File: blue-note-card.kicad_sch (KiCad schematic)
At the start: 22 parts, among them J17 N_GR1, J3 MDT420E01001, J7 SF72S006VBAR2500

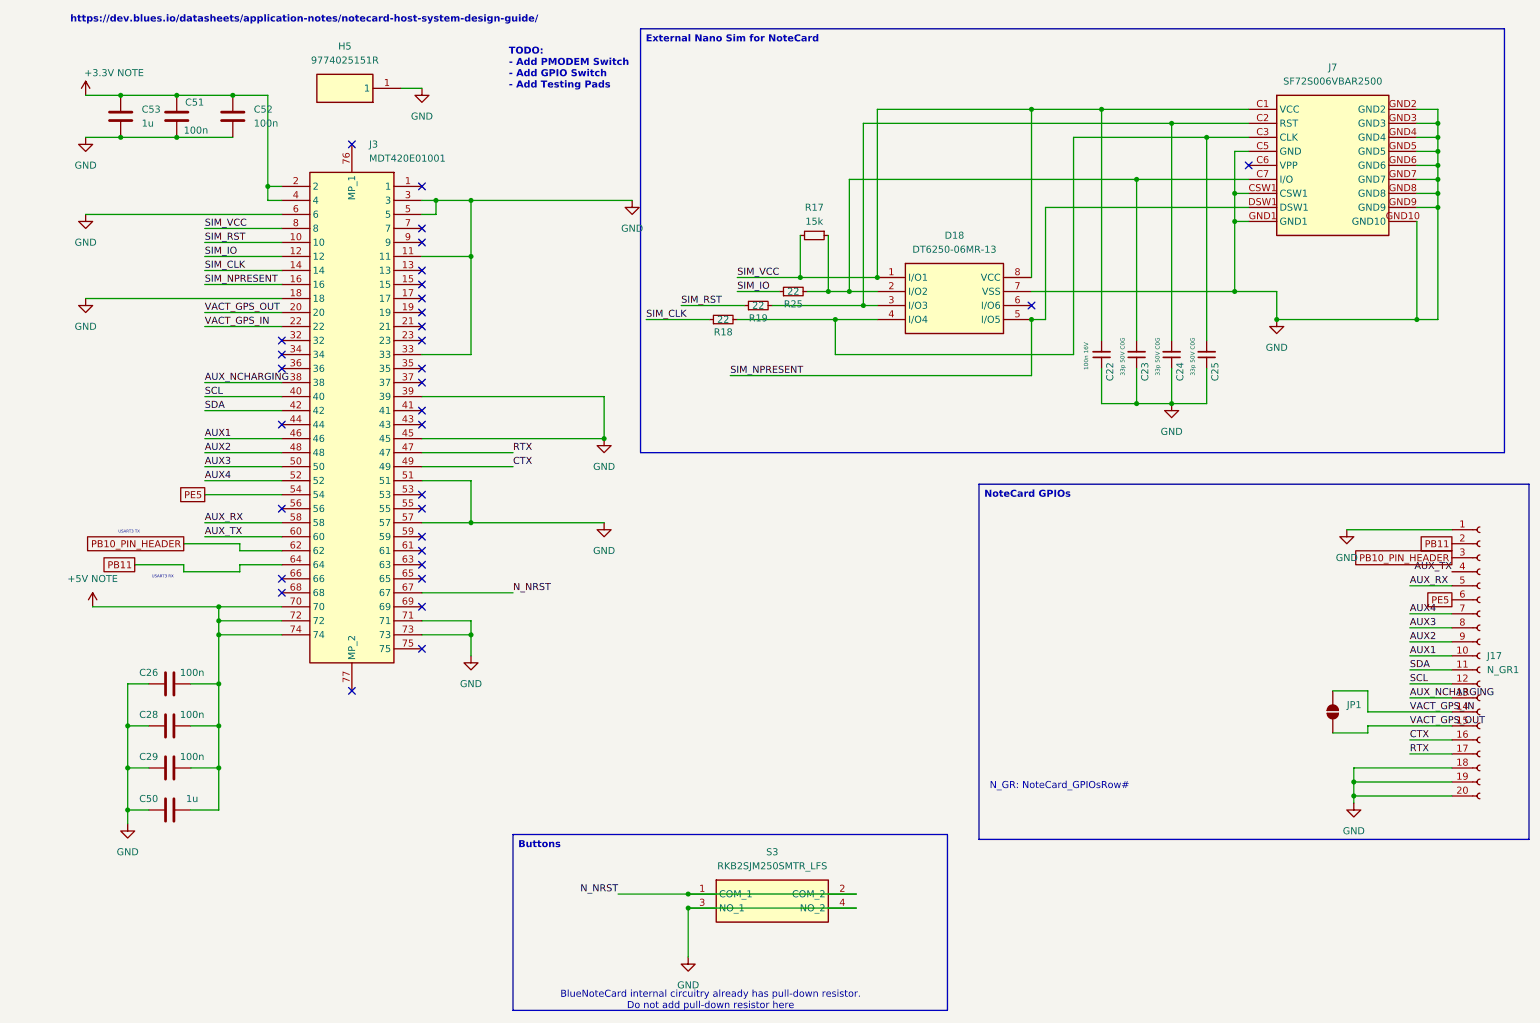
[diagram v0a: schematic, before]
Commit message: Added AUX_EN, I2C com to Blues, LED labels
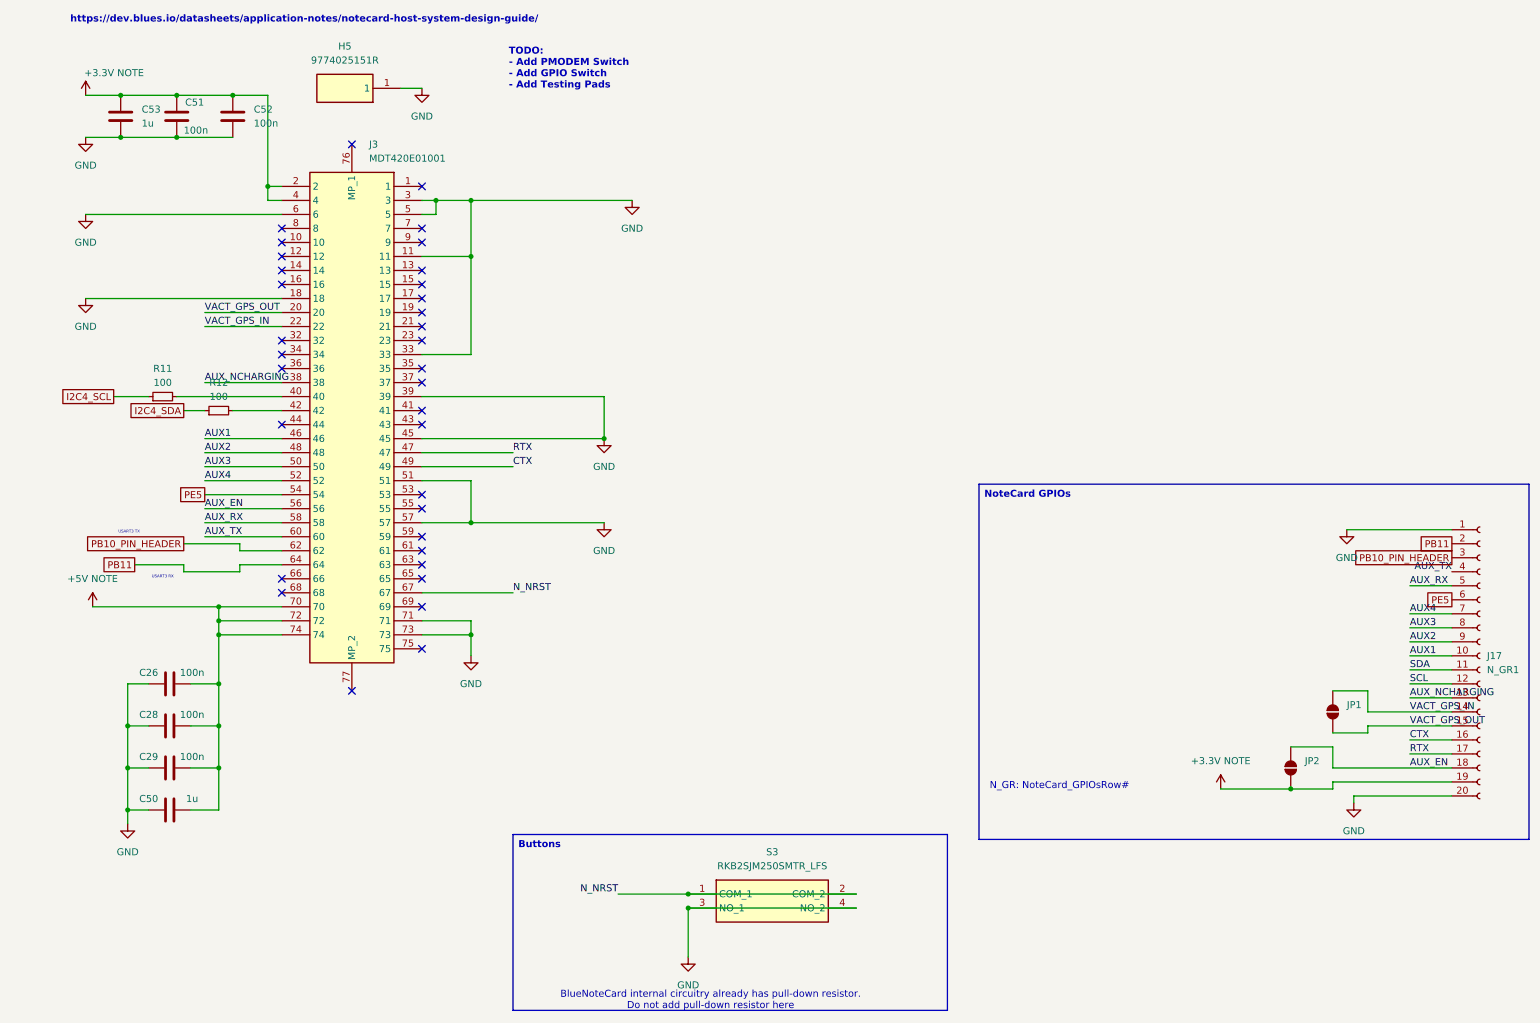
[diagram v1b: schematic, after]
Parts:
- removed C22: 100n 16V, Capacitor_SMD:C_0603_1608Metric_Pad1.08x0.95mm_HandSolder, symbol Device:C_Small
- removed C23, C24, C25: 33p 50V C0G, Capacitor_SMD:C_0603_1608Metric_Pad1.08x0.95mm_HandSolder, symbol Device:C_Small
- removed D18: DT6250-06MR-13, SamacSys_Parts:SOP65P490X110-8N, symbol SamacSys_Parts:DT6250-06MR-13
- removed J7: SF72S006VBAR2500, SamacSys_Parts:SF72S006VBAR2500, symbol SamacSys_Parts:SF72S006VBAR2500
- removed R17: 15k, Resistor_SMD:R_0805_2012Metric_Pad1.20x1.40mm_HandSolder, symbol Device:R_Small
- removed R18, R19, R25: 22, Resistor_SMD:R_0603_1608Metric_Pad0.98x0.95mm_HandSolder, symbol Device:R_Small
- added JP2: SolderJumper_2_Open, Jumper:SolderJumper-2_P1.3mm_Open_RoundedPad1.0x1.5mm, symbol Jumper:SolderJumper_2_Open
- added R11, R12: 100, Resistor_SMD:R_0603_1608Metric_Pad0.98x0.95mm_HandSolder, symbol Device:R_Small
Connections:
- net +3.3V NOTE: now also J17.19 (Pin_19), JP2.2 (B)
- net GND: no longer J17.18 (Pin_18), J17.19 (Pin_19)
- net SCL: no longer J3.40
- net SDA: no longer J3.42
- net AUX_EN: now reaches J3.56
- net AUX_EN: now also J17.18 (Pin_18), JP2.1 (A)
- net SIM_CLK: no longer names the net of J3.14
- net SIM_IO: no longer names the net of J3.12
- net SIM_NPRESENT: no longer names the net of J3.16
- net SIM_RST: no longer names the net of J3.10
- net SIM_VCC: no longer names the net of J3.8
- new net: J3.40, R11.2
- new net: J3.42, R12.2
- new net I2C4_SCL: R11.1
- new net I2C4_SDA: R12.1
- no-connect marks 32 -> 34

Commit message: Added module LEDs, I2C for Blues Com
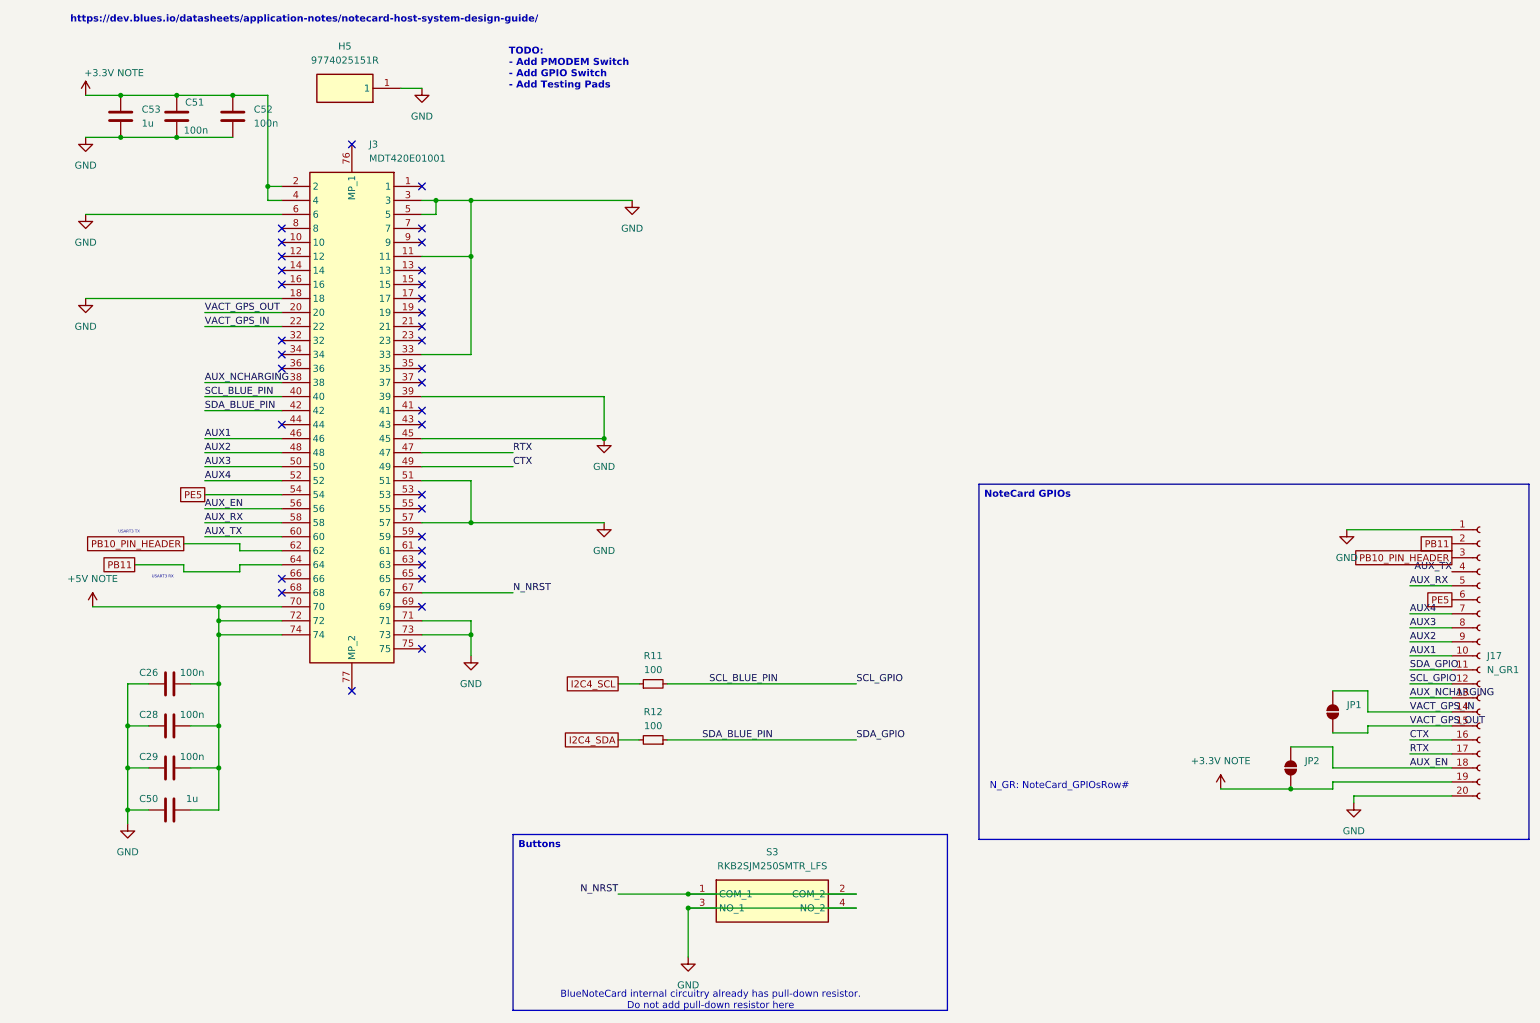
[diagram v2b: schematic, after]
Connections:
- net SCL is gone; now on net SCL_BLUE_PIN: J17.12 (Pin_12)
- net SDA is gone; now on net SDA_BLUE_PIN: J17.11 (Pin_11)
- net I2C4_SDA: now also R12.2; no longer R12.1
- net SCL_BLUE_PIN: now reaches J3.40, R11.2
- net SDA_BLUE_PIN: now reaches J3.42
- net SDA_BLUE_PIN: now also R12.1; no longer R12.2
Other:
- moved on the sheet: R11, R12
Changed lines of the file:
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@@
-	(wire
-		(pts
-			(xy 36.83 87.63) (xy 40.64 87.63)
-		)
-		(stroke
-			(width 0)
-			(type default)
-		)
-	)
 	(wire
 		(pts
@@
 	(wire
 		(pts
+			(xy 115.57 137.16) (xy 119.38 137.16)
+		)
+		(stroke
+			(width 0)
+			(type default)
+		)
+	)
+	(wire
+		(pts
 			(xy 54.61 102.87) (xy 40.64 102.87)
 		)
@@
 	(wire
 		(pts
-			(xy 35.56 85.09) (xy 54.61 85.09)
-		)
-		(stroke
-			(width 0)
-			(type default)
-		)
-	)
-	(wire
-		(pts
 			(xy 80.01 120.65) (xy 96.52 120.65)
 		)
@@
 	(wire
 		(pts
+			(xy 54.61 85.09) (xy 40.64 85.09)
+		)
+		(stroke
+			(width 0)
+			(type default)
+		)
+	)
+	(wire
+		(pts
+			(xy 124.46 137.16) (xy 158.75 137.16)
+		)
+		(stroke
+			(width 0)
+			(type default)
+		)
+	)
+	(wire
+		(pts
 			(xy 88.9 128.27) (xy 88.9 132.08)
 		)
@@
 	(wire
 		(pts
+			(xy 115.57 147.32) (xy 119.38 147.32)
+		)
+		(stroke
+			(width 0)
+			(type default)
+		)
+	)
+	(wire
+		(pts
 			(xy 40.64 72.39) (xy 54.61 72.39)
 		)
@@
 	(wire
 		(pts
-			(xy 24.13 85.09) (xy 30.48 85.09)
-		)
-		(stroke
-			(width 0)
-			(type default)
-		)
-	)
-	(wire
-		(pts
 			(xy 80.01 92.71) (xy 113.03 92.71)
 		)
@@
 	(wire
 		(pts
+			(xy 40.64 87.63) (xy 54.61 87.63)
+		)
+		(stroke
+			(width 0)
+			(type default)
+		)
+	)
+	(wire
+		(pts
 			(xy 88.9 59.69) (xy 88.9 49.53)
 		)
@@
 	(wire
 		(pts
-			(xy 45.72 87.63) (xy 54.61 87.63)
-		)
-		(stroke
-			(width 0)
-			(type default)
-		)
-	)
-	(wire
-		(pts
 			(xy 25.4 38.1) (xy 19.05 38.1)
 		)
@@
 	(wire
 		(pts
+			(xy 124.46 147.32) (xy 158.75 147.32)
+		)
+		(stroke
+			(width 0)
+			(type default)
+		)
+	)
+	(wire
+		(pts
 			(xy 54.61 97.79) (xy 40.64 97.79)
 		)
@@
 			(width 0)
 			(type default)
+		)
+	)
+	(label "SCL_BLUE_PIN"
+		(at 132.08 137.16 0)
+		(effects
+			(font
+				(size 1.27 1.27)
+			)
+			(justify left bottom)
 		)
 	)
@@
 		)
 	)
+	(label "SCL_GPIO"
+		(at 158.75 137.16 0)
+		(effects
+			(font
+				(size 1.27 1.27)
+			)
+			(justify left bottom)
+		)
+	)
 	(label "VACT_GPS_IN"
 		(at 40.64 72.39 0)
@@
 		)
 	)
-	(label "SCL"
+	(label "SCL_GPIO"
 		(at 259.08 137.16 0)
 		(effects
@@
 		)
 	)
-	(label "SDA"
+	(label "SDA_GPIO"
 		(at 259.08 134.62 0)
 		(effects
@@
 		)
 	)
+	(label "SDA_GPIO"
+		(at 158.75 147.32 0)
+		(effects
+			(font
+				(size 1.27 1.27)
+			)
+			(justify left bottom)
+		)
+	)
 	(label "AUX_TX"
 		(at 266.7 116.84 180)
@@
 		)
 	)
+	(label "SDA_BLUE_PIN"
+		(at 130.81 147.32 0)
+		(effects
+			(font
+				(size 1.27 1.27)
+			)
+			(justify left bottom)
+		)
+	)
 	(label "AUX_RX"
 		(at 259.08 119.38 0)
@@
 	(label "AUX1"
 		(at 259.08 132.08 0)
+		(effects
+			(font
+				(size 1.27 1.27)
+			)
+			(justify left bottom)
+		)
+	)
+	(label "SDA_BLUE_PIN"
+		(at 40.64 87.63 0)
+		(effects
+			(font
+				(size 1.27 1.27)
+			)
+			(justify left bottom)
+		)
+	)
+	(label "SCL_BLUE_PIN"
+		(at 40.64 85.09 0)
 		(effects
 			(font
@@
 	(global_label "I2C4_SDA"
 		(shape passive)
-		(at 36.83 87.63 180)
+		(at 115.57 147.32 180)
 		(fields_autoplaced yes)
 		(effects
@@
 		)
 		(property "Intersheetrefs" "${INTERSHEET_REFS}"
-			(at 26.1266 87.63 0)
+			(at 104.8666 147.32 0)
 			(effects
 				(font
@@
 	(global_label "I2C4_SCL"
 		(shape passive)
-		(at 24.13 85.09 180)
+		(at 115.57 137.16 180)
 		(fields_autoplaced yes)
 		(effects
@@
 		)
 		(property "Intersheetrefs" "${INTERSHEET_REFS}"
-			(at 13.4871 85.09 0)
+			(at 104.9271 137.16 0)
 			(effects
 				(font
@@
 	(symbol
 		(lib_id "Device:R_Small")
-		(at 33.02 85.09 90)
+		(at 121.92 137.16 90)
 		(unit 1)
 		(exclude_from_sim no)
@@
 		(fields_autoplaced yes)
 		(property "Reference" "R11"
-			(at 33.02 80.01 90)
+			(at 121.92 132.08 90)
 			(effects
 				(font
@@
 		)
 		(property "Value" "100"
-			(at 33.02 82.55 90)
+			(at 121.92 134.62 90)
 			(effects
 				(font
@@
 		)
 		(property "Footprint" "Resistor_SMD:R_0603_1608Metric_Pad0.98x0.95mm_HandSolder"
-			(at 33.02 85.09 0)
+			(at 121.92 137.16 0)
 			(effects
 				(font
@@
 		)
 		(property "Datasheet" "~"
-			(at 33.02 85.09 0)
+			(at 121.92 137.16 0)
 			(effects
 				(font
@@
 		)
 		(property "Description" "Resistor, small symbol"
-			(at 33.02 85.09 0)
+			(at 121.92 137.16 0)
 			(effects
 				(font
@@
 	(symbol
 		(lib_id "Device:R_Small")
-		(at 43.18 87.63 90)
+		(at 121.92 147.32 270)
+		(mirror x)
 		(unit 1)
 		(exclude_from_sim no)
@@
 		(on_board yes)
 		(dnp no)
-		(fields_autoplaced yes)
 		(property "Reference" "R12"
-			(at 43.18 82.55 90)
+			(at 121.92 142.24 90)
 			(effects
 				(font
@@
 		)
 		(property "Value" "100"
-			(at 43.18 85.09 90)
+			(at 121.92 144.78 90)
 			(effects
 				(font
@@
 		)
 		(property "Footprint" "Resistor_SMD:R_0603_1608Metric_Pad0.98x0.95mm_HandSolder"
-			(at 43.18 87.63 0)
+			(at 121.92 147.32 0)
 			(effects
 				(font
@@
 		)
 		(property "Datasheet" "~"
-			(at 43.18 87.63 0)
+			(at 121.92 147.32 0)
 			(effects
 				(font
@@
 		)
 		(property "Description" "Resistor, small symbol"
-			(at 43.18 87.63 0)
-			(effects
-				(font
+			(at 121.92 147.32 0)
+			(effects
+				(font

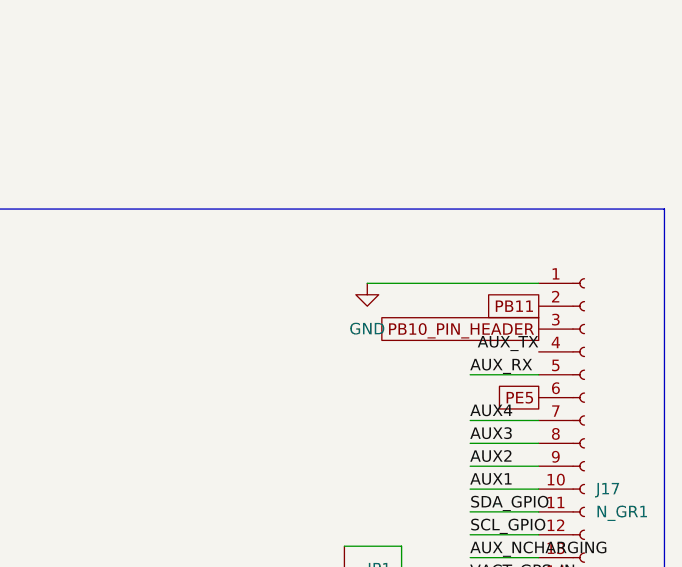
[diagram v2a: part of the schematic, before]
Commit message: Fixed SD Card layout
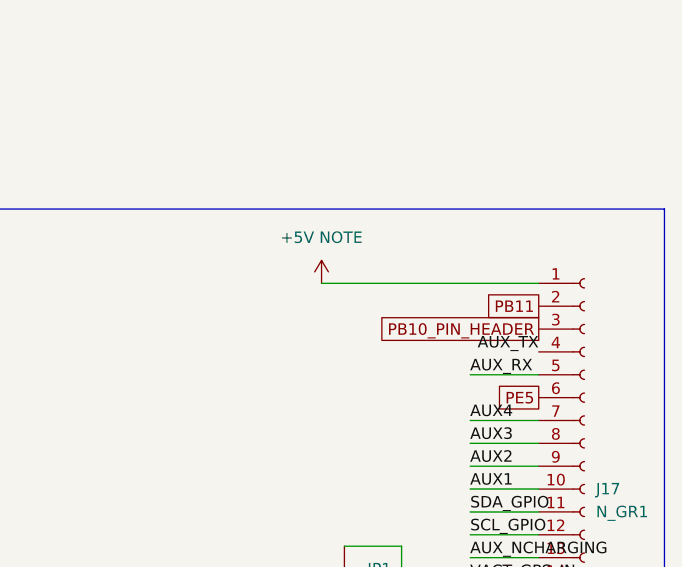
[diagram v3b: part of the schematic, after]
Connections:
- net +5V NOTE: now also J17.1 (Pin_1)
- net GND: no longer J17.1 (Pin_1)
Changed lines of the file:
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@@
+	(wire
+		(pts
+			(xy 242.57 109.22) (xy 266.7 109.22)
+		)
+		(stroke
+			(width 0)
+			(type default)
+		)
+	)
 	(wire
 		(pts
@@
 		(pts
 			(xy 20.32 123.19) (xy 43.18 123.19)
-		)
-		(stroke
-			(width 0)
-			(type default)
-		)
-	)
-	(wire
-		(pts
-			(xy 247.65 109.22) (xy 266.7 109.22)
 		)
 		(stroke
@@
 				(justify right)
 				(hide yes)
+			)
+		)
+	)
+	(symbol
+		(lib_id "power:+5V")
+		(at 242.57 109.22 0)
+		(unit 1)
+		(exclude_from_sim no)
+		(in_bom yes)
+		(on_board yes)
+		(dnp no)
+		(fields_autoplaced yes)
+		(property "Reference" "#PWR079"
+			(at 242.57 113.03 0)
+			(effects
+				(font
+					(size 1.27 1.27)
+				)
+				(hide yes)
+			)
+		)
+		(property "Value" "+5V NOTE"
+			(at 242.57 104.14 0)
+			(effects
+				(font
+					(size 1.27 1.27)
+				)
+			)
+		)
+		(property "Footprint" ""
+			(at 242.57 109.22 0)
+			(effects
+				(font
+					(size 1.27 1.27)
+				)
+				(hide yes)
+			)
+		)
+		(property "Datasheet" ""
+			(at 242.57 109.22 0)
+			(effects
+				(font
+					(size 1.27 1.27)
+				)
+				(hide yes)
+			)
+		)
+		(property "Description" "Power symbol creates a global label with name \"+5V\""
+			(at 242.57 109.22 0)
+			(effects
+				(font
+					(size 1.27 1.27)
+				)
+				(hide yes)
+			)
+		)
+		(pin "1"
+		)
+		(instances
+			(project ""
+				(path "/32c2c747-0685-4927-b759-a1d2bc91875e/a361650e-b291-433d-8ba6-4be6ed8b8d80"
+					(reference "#PWR079")
+					(unit 1)
+				)
 			)
 		)
@@
 					(unit 1)
 				)
-			)
-		)
-	)
-	(symbol
-		(lib_id "power:GND")
-		(at 247.65 109.22 0)
-		(unit 1)
-		(exclude_from_sim no)
-		(in_bom yes)
-		(on_board yes)
-		(dnp no)
-		(fields_autoplaced yes)
-		(property "Reference" "#PWR055"
-			(at 247.65 115.57 0)
-			(effects
-				(font
-					(size 1.27 1.27)
-				)
-				(hide yes)
-			)
-		)
-		(property "Value" "GND"
-			(at 247.65 114.3 0)
-			(effects
-				(font
-					(size 1.27 1.27)
-				)
-			)
-		)
-		(property "Footprint" ""
-			(at 247.65 109.22 0)
-			(effects
-				(font
-					(size 1.27 1.27)
-				)
-				(hide yes)
-			)
-		)
-		(property "Datasheet" ""
-			(at 247.65 109.22 0)
-			(effects
-				(font
-					(size 1.27 1.27)
-				)
-				(hide yes)
-			)
-		)
-		(property "Description" "Power symbol creates a global label with name \"GND\" , ground"
-			(at 247.65 109.22 0)
-			(effects
-				(font
-					(size 1.27 1.27)
-				)
-				(hide yes)
-			)
-		)
-		(pin "1"
-		)
-		(instances
-			(project ""
-				(path "/32c2c747-0685-4927-b759-a1d2bc91875e/a361650e-b291-433d-8ba6-4be6ed8b8d80"
-					(reference "#PWR055")
-					(unit 1)
-				)
